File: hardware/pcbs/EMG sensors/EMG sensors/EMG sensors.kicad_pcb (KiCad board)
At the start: 4 copper layers, 90.3 x 73 mm, 28 parts, among them IC1 INA128, U6 OPA2188AIDR, U7 OPA188AIDR

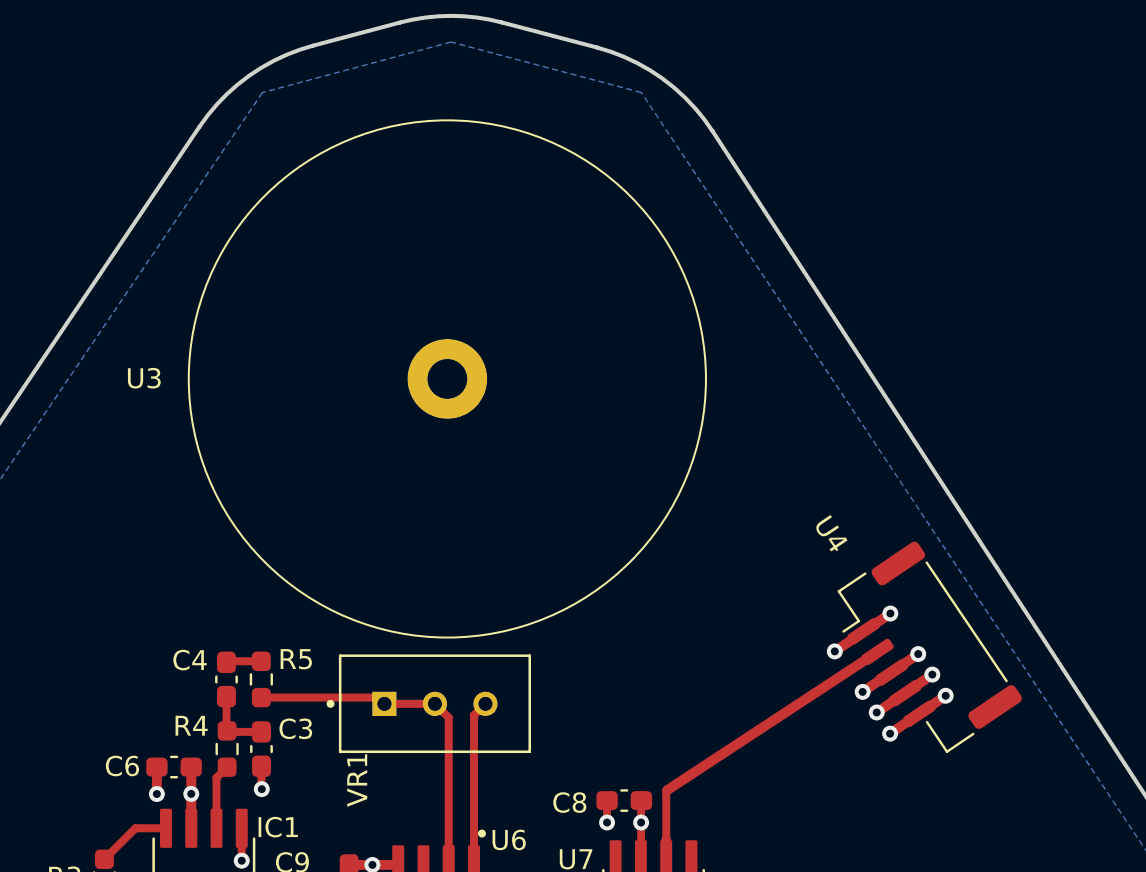
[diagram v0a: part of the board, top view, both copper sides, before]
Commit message: Voltage supply of sEMG & ADC
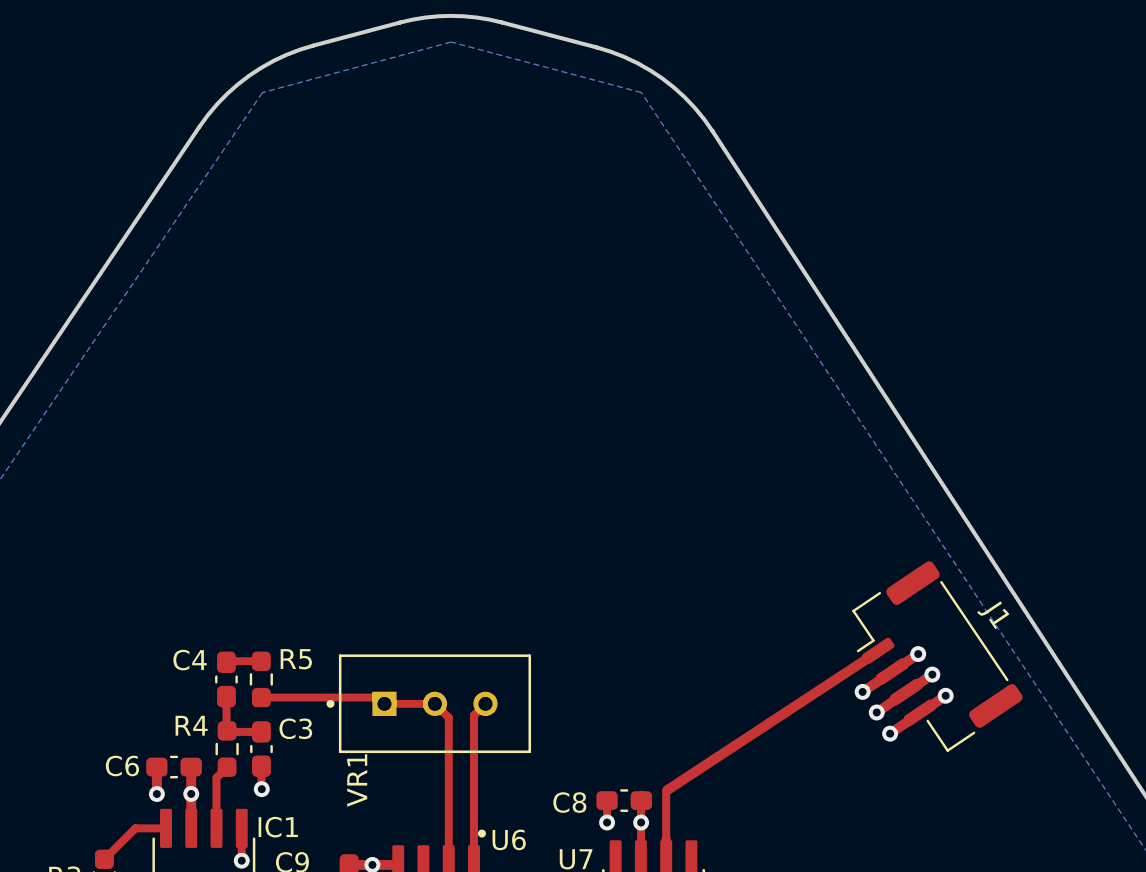
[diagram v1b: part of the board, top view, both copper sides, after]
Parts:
- removed U3: ~, EMG:EMG_Snap_4mm
- removed U4: ~, Connector_JST:JST_GH_BM05B-GHS-TBT_1x05-1MP_P1.25mm_Vertical
- added J1: Conn_01x04_Pin, Connector_JST:JST_GH_BM04B-GHS-TBT_1x04-1MP_P1.25mm_Vertical, F.Cu at (157.5, 100.3)
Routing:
- net Ref: vias 16 -> 14

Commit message: EMG sensor v0.2
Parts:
- added J2: Conn_01x01_Pin, Connectors:DIN_Male_1PIN_1.5mm, F.Cu at (110.9, 103.6)
- U1, U2: moved to B.Cu
- moved U2 16.2 mm to (151.0, 110.6)
- moved U1 15.3 mm to (112.0, 110.5)
- moved J1 12.5 mm to (145.1, 102.2), turned to 0 degrees
- moved C8 2.18 mm to (139.8, 107.4)
- moved R6 2.13 mm to (129.5, 119.7)
- moved R5 1.50 mm to (125.2, 101.6)
- moved R2 1.50 mm to (124.0, 116.4)
- moved C9 1.50 mm to (126.8, 113.2)
- moved IC1 1.50 mm to (122.3, 111.6)
- moved R3 1.50 mm to (117.3, 111.6)
- moved C3 1.50 mm to (125.2, 105.1)
- moved C4 1.50 mm to (123.5, 101.6)
- moved C6 1.50 mm to (120.8, 106.0)
- moved R1 1.50 mm to (120.6, 116.4)
- moved R4 1.50 mm to (123.5, 105.1)
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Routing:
- net INVERTED: track 30.0 -> 24.0 mm
- net Vin2: track 46.4 -> 42.0 mm
- net /+5.5V: track 9.04 -> 12.7 mm
- net Ref: track 18.6 -> 21.6 mm
- net /-5.5V: track 8.53 -> 11.5 mm
- net Vin1: track 22.8 -> 25.5 mm
- net Net-(U6--INA): track 17.3 -> 15.9 mm
- net Net-(D1-A): track 8.92 -> 7.57 mm
- net /AEMG: track 9.34 -> 10.2 mm
- net Net-(U7--IN): track 18.9 -> 18.2 mm
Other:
- board size 90.3 x 73 mm -> 65 x 26 mm
- board text added: "*"
- board text added: "* * * * * * * * * * * * * * * * * * * * * * * * *"

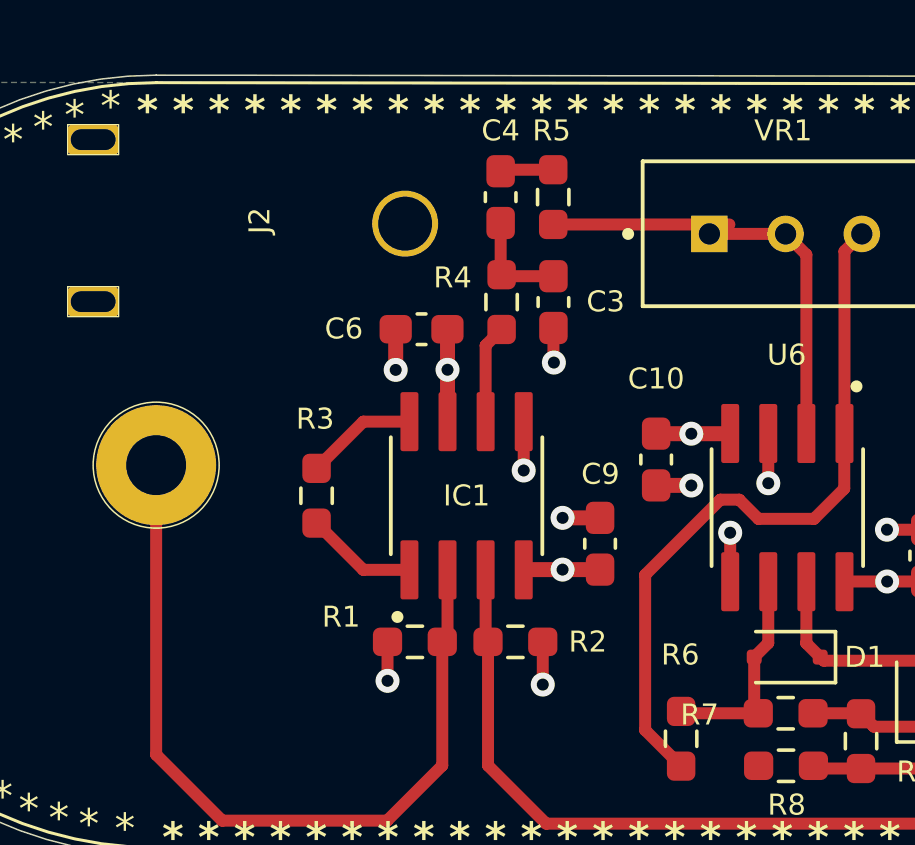
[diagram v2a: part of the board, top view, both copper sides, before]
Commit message: sEMG sensors v0.3
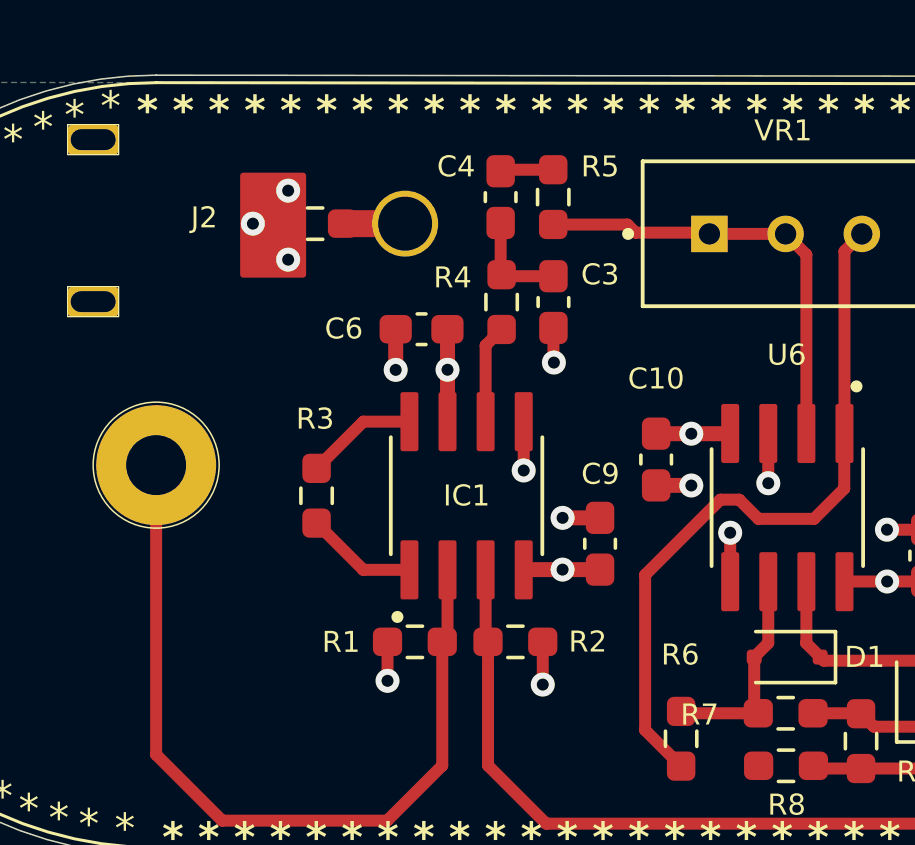
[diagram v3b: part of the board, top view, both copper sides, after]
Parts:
- added R11: 1M, Resistor_SMD:R_0603_1608Metric_Pad0.98x0.95mm_HandSolder, F.Cu at (117.3, 102.5)
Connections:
- J1 pad 2: Ref -> GND
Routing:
- net GND: track 0.00 -> 3.00 mm, vias 0 -> 5
- net Net-(U6--INA): track 15.9 -> 14.9 mm
- net Ref: track 21.6 -> 20.7 mm, vias 14 -> 12
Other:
- board text added: "SensaLimb sEMG"

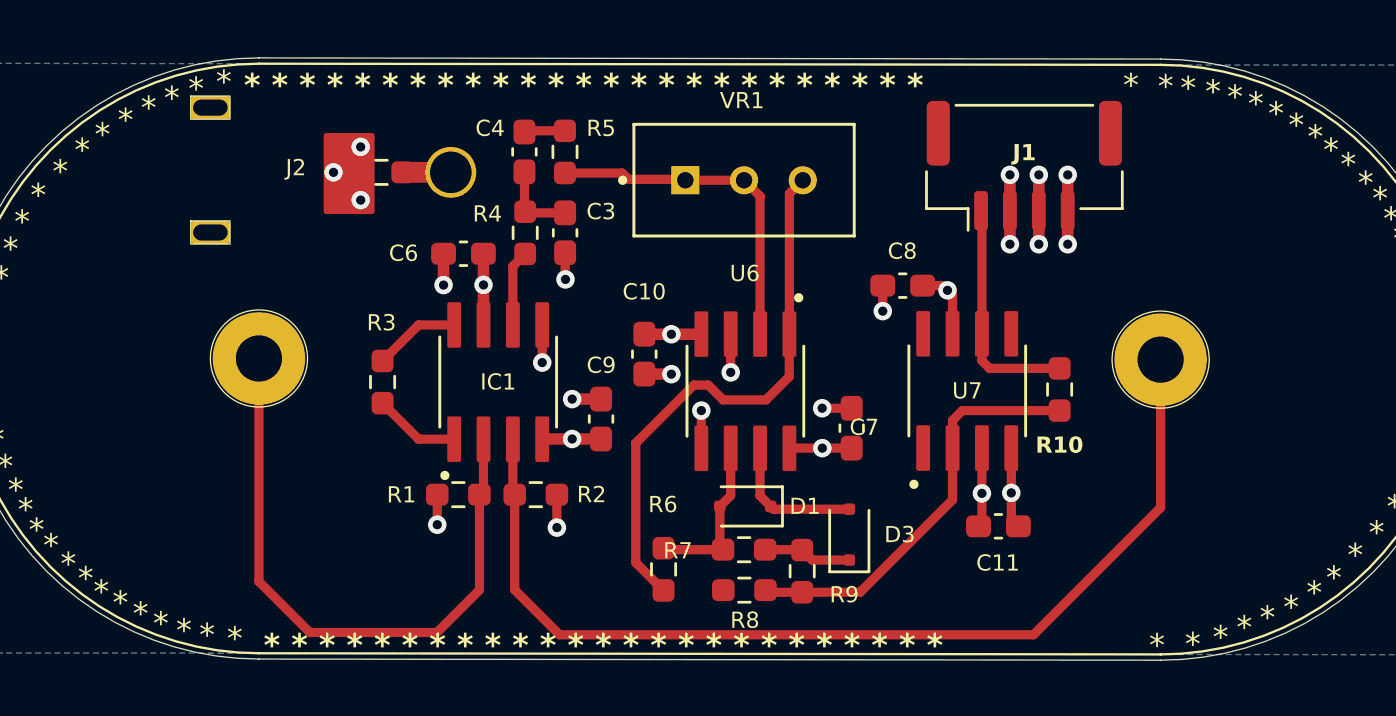
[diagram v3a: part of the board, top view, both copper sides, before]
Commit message: Fixes
sEMG - minor
Voltage supply... - major but not fixed
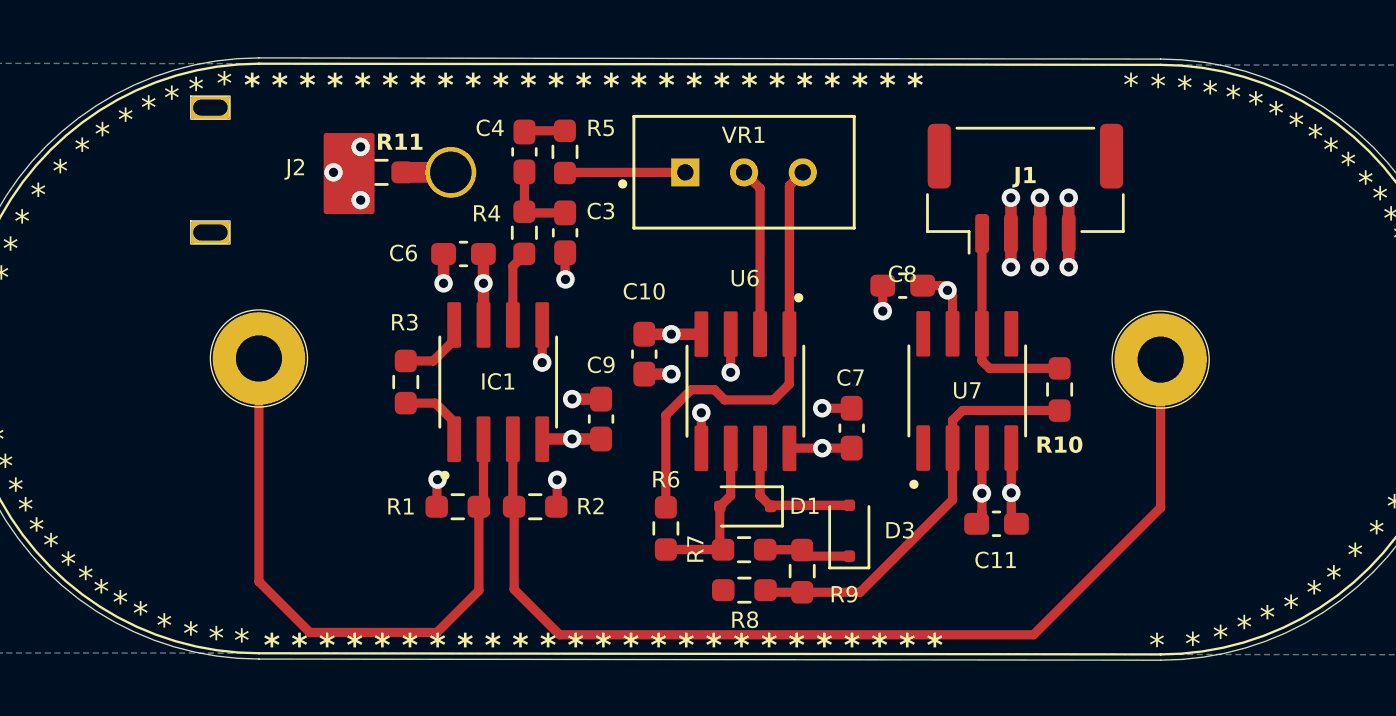
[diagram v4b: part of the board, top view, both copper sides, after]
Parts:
- moved R6 1.77 mm to (129.6, 117.9), turned to -90 degrees
- moved R3 1.00 mm to (118.3, 111.6)
- moved J1 0.99 mm to (145.2, 103.2)
- moved R1 0.52 mm to (120.6, 117.0)
- moved R2 0.52 mm to (124.0, 117.0)
- moved VR1 0.34 mm to (133.0, 102.5)
- moved D3 0.17 mm to (137.5, 118.0)
- moved C11 0.14 mm to (143.9, 117.7)
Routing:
- net INVERTED: track 24.0 -> 19.6 mm
- net Net-(U6--INA): track 14.9 -> 12.6 mm
- net /AEMG: track 10.2 -> 9.29 mm
- net Net-(IC1-Pad8): track 3.74 -> 3.12 mm
- net Net-(IC1-Pad1): track 3.74 -> 3.18 mm
- net Ref: track 20.7 -> 20.1 mm
